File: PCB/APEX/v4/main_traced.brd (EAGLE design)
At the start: 76.2 x 52.7 mm, 22 parts

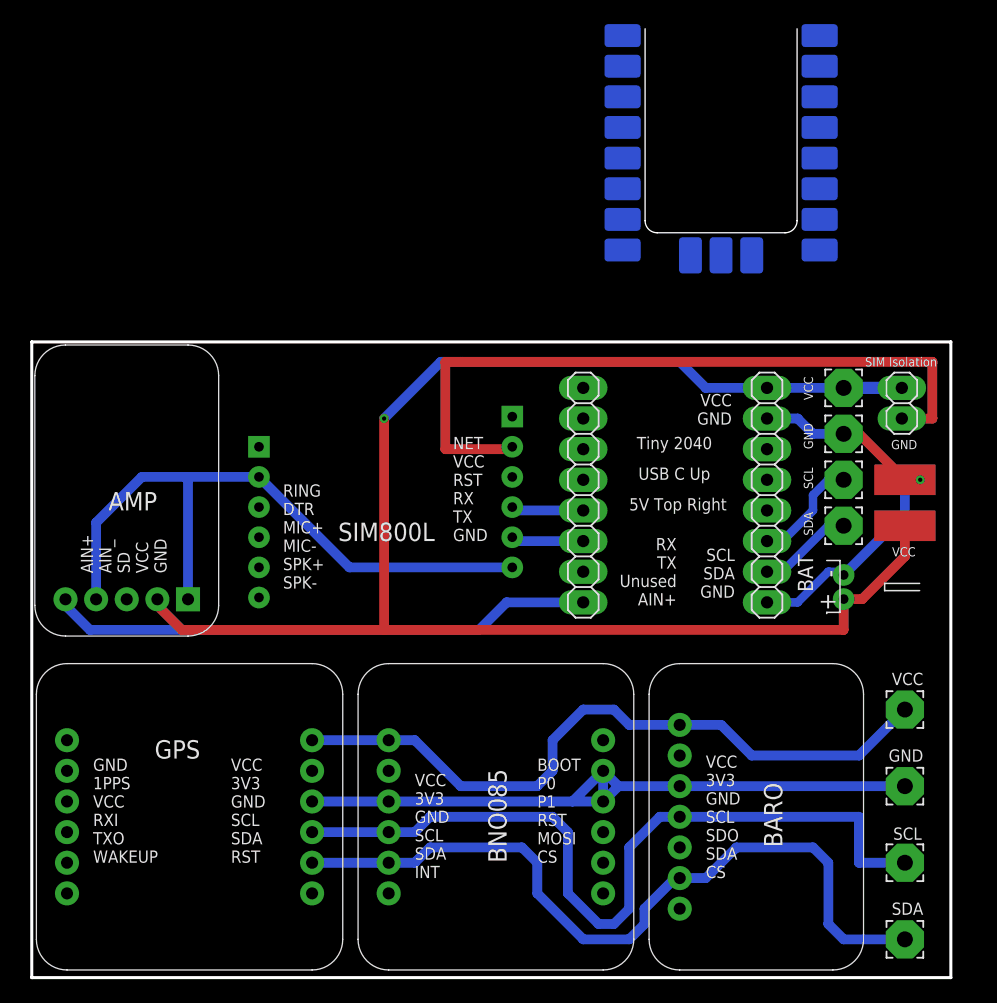
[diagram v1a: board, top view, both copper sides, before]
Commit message: ground pour
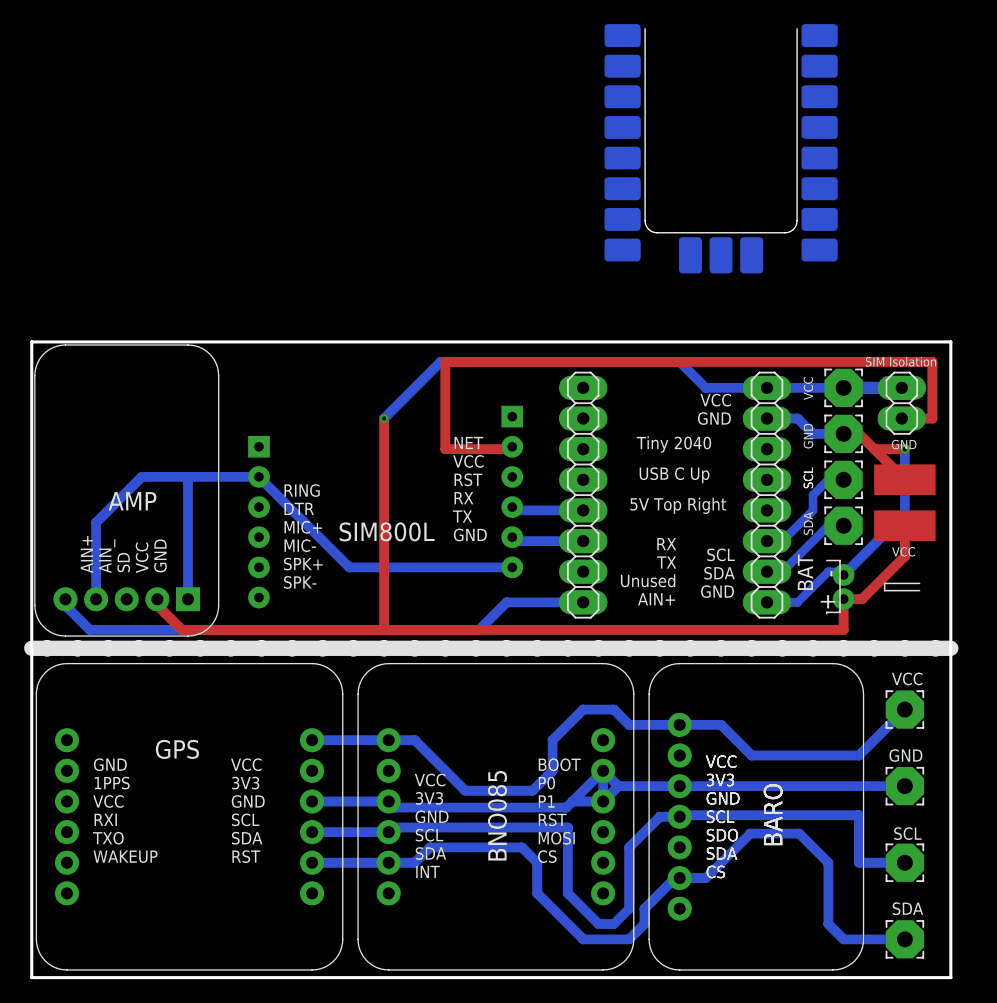
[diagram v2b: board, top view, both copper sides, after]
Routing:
- net GND: track 145.7 -> 149.9 mm
- net SDA: track 72.3 -> 73.2 mm
- added copper zone on layer 1, net GND
- added copper zone on layer 16, net GND

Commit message: add labels
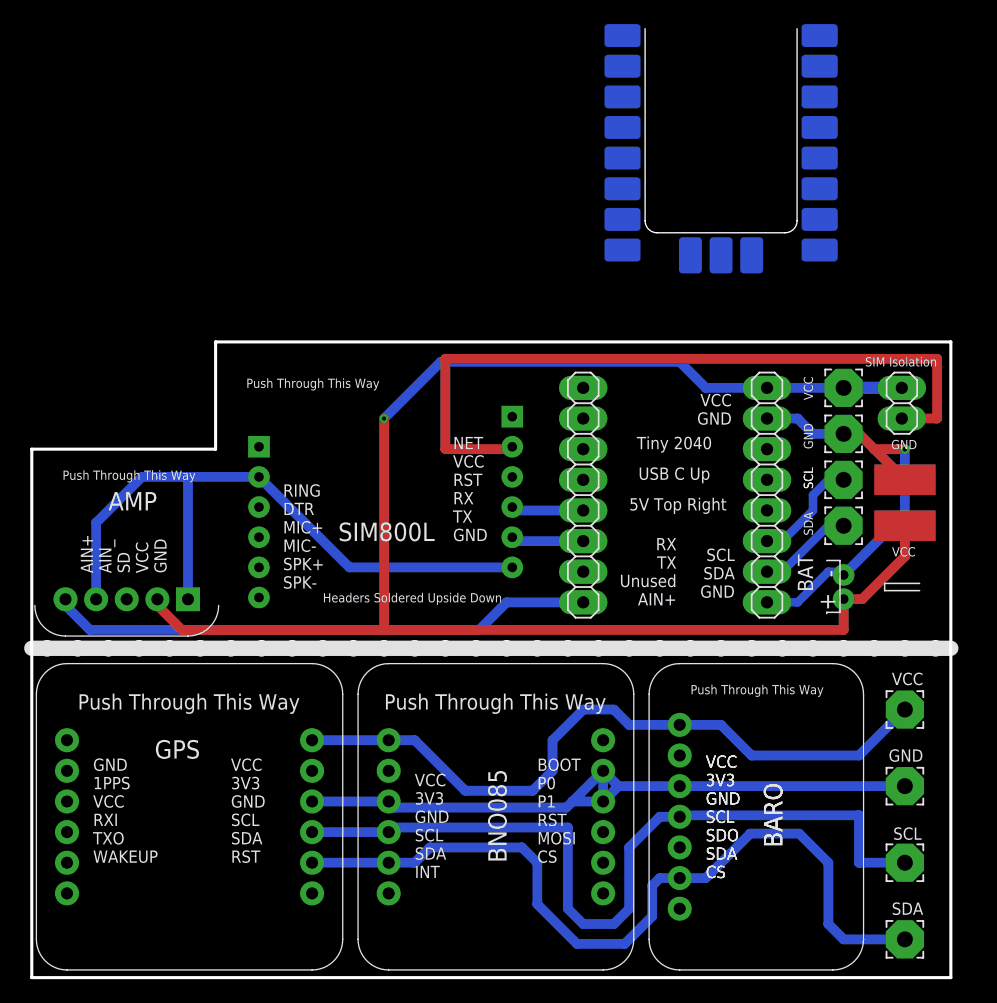
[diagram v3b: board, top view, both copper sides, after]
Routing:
- net SDA: track 73.2 -> 75.2 mm
- net SIMPOW: track 60.5 -> 61.8 mm
- net SCL: track 75.7 -> 76.4 mm
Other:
- outline, holes or cut-outs redrawn
- board text added: "APEX Comms"
- board text added: "APEX Sensor Board"
- board text added: "Altitude Record Team"
- board text added: "GND VCC SD AIN- AIN+"
- board text added: "Headers Soldered Upside Down"
- board text added: "Push Through This Way"
- board text added: "Shrey Bohra, Rohit Singh, Jason Hon, Akshat Tripathi, Harry Allcock Julian Ting, Nathanael Jenkins, Rohin Nayar, Tash Tanim, Kwan Yiu Tam"
